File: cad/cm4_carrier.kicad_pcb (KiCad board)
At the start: 2 copper layers, 100 x 80 mm, 24 parts, among them J1 5V_IN, J2 CM4, J3 RS485, J4 USB_DEBUG, J5 I2C, J6 SPI, J7 GPIO, Q1 SI2301, U1 MAX3485, U2 CP2102N

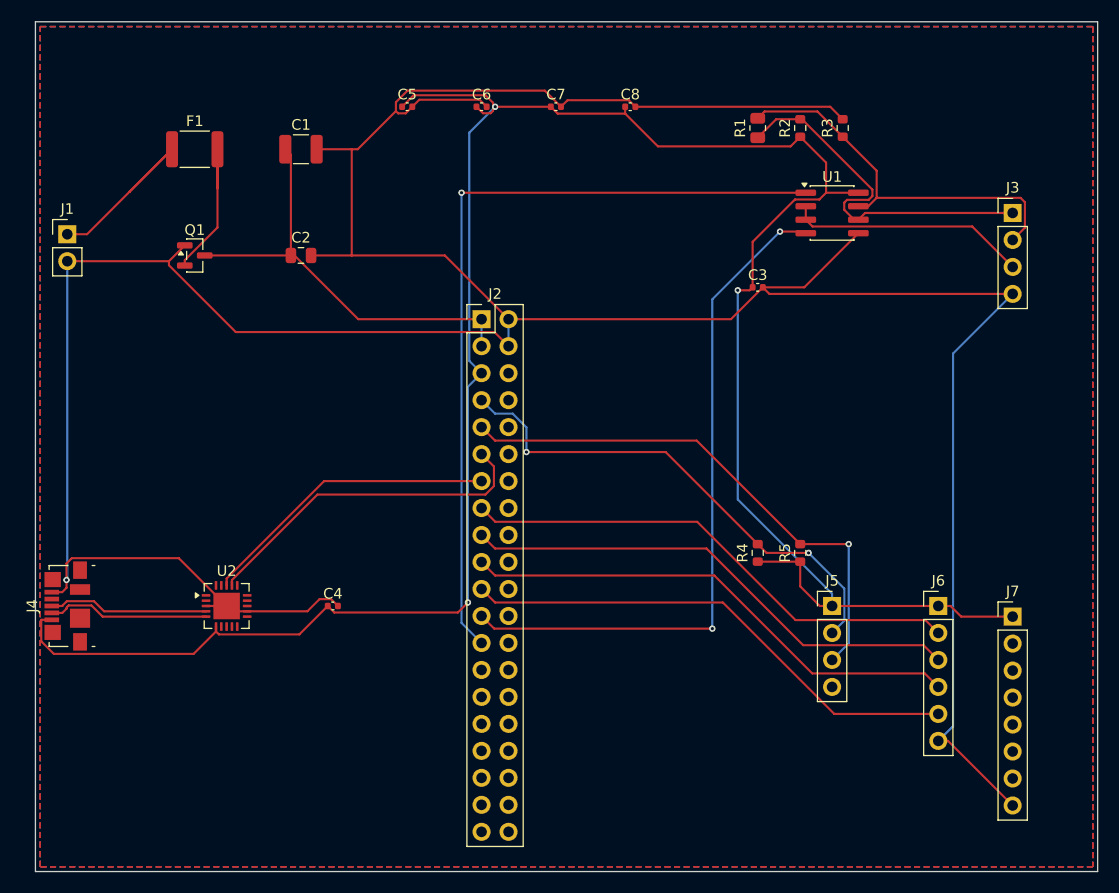
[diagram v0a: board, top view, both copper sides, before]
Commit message: ♻️ refactor: split pcb_placement.yaml from layout_spec, skill owns placement
- layout_spec.yaml is human config, pcb_placement.yaml is AI-generated
- place_pcb.py simplified to read/place/clear — no compute_placement algorithm
- /layout-pcb skill reads netlist connectivity and places components intelligently
- place_pcb.py clears stale traces before placing (root cause of prior DRC failures)
- Full clean-slate pipeline: 0 violations, 0 unconnected on first attempt

Co-Authored-By: Claude Opus 4.6 (1M context) <noreply@anthropic.com>
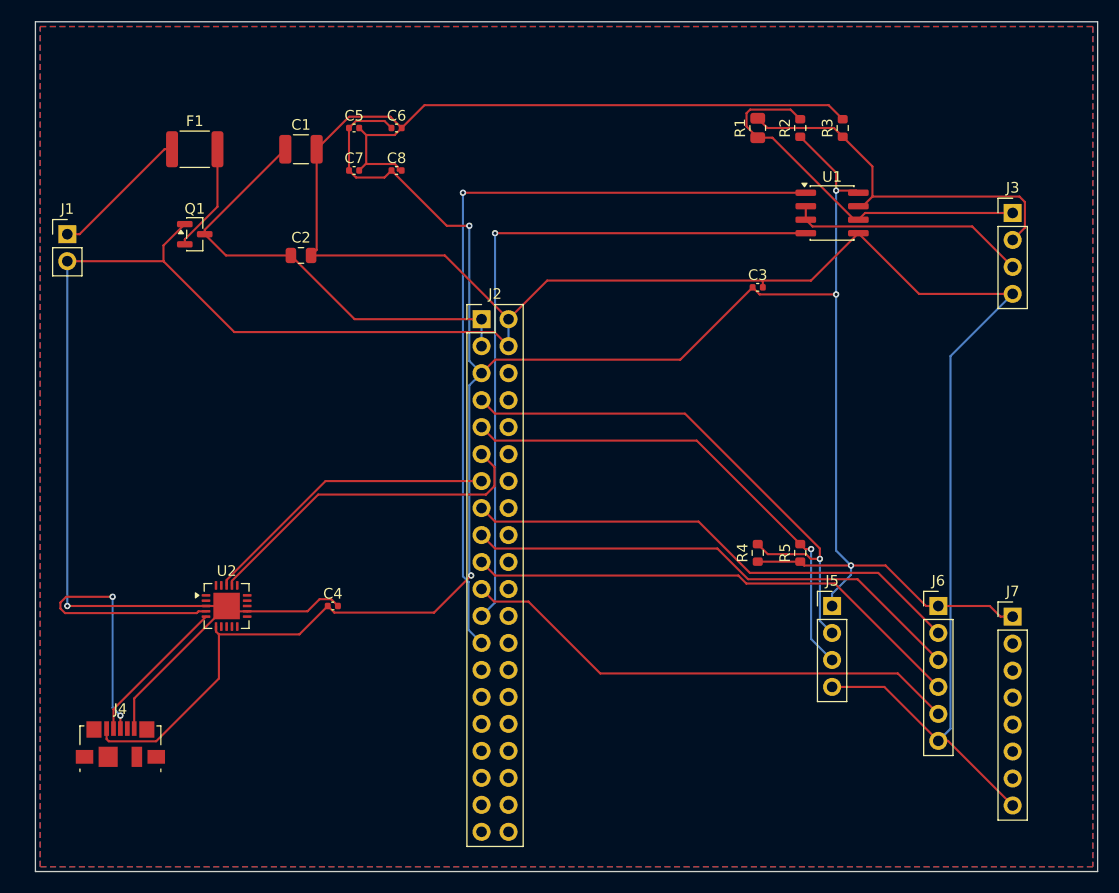
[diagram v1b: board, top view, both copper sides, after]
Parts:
- moved C8 22.8 mm to (134.0, 94.0)
- moved C7 19.9 mm to (130.0, 94.0)
- moved J4 13.9 mm to (108.0, 148.0), turned to 0 degrees
- moved C6 8.25 mm to (134.0, 90.0)
- moved C5 5.39 mm to (130.0, 90.0)
- moved Q1 2.00 mm to (115.0, 100.0)
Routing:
- net GND: track 323.1 -> 342.3 mm
- net /USB_DP: track 15.1 -> 32.4 mm, vias 0 -> 2
- net +3V3: track 223.9 -> 214.4 mm, vias 3 -> 5
- net Net-(Q1-S): track 16.2 -> 10.2 mm
- net /5V_IN: track 18.8 -> 13.2 mm
- net /SDA: track 47.5 -> 52.5 mm, vias 2 -> 1
- net /SCL: track 50.7 -> 47.0 mm
- net +5V: track 41.6 -> 43.1 mm
- net /USB_DM: track 15.3 -> 14.1 mm
- net /RS485_TX: track 64.7 -> 65.8 mm, vias 2 -> 1
- net /RS485_A: track 35.0 -> 35.8 mm
- net /RS485_B: track 36.5 -> 35.8 mm
